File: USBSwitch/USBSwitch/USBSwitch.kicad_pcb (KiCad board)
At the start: 2 copper layers, 41 x 32 mm, 17 parts, among them J1 Conn_01x01_Female, J2 Conn_01x01_Female, J3 USB_A, J4 USB_B_Micro

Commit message: Update USBSwitch
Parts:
- removed REF**: Jitter Icon, Jitter_Logos:Symbol_Jitter-Icon_CopperAndSilkScreenTop
- removed REF**: KiCAD Logo, Symbol:Symbol_KiCAD-Logo_CopperAndSilkScreenTop
- added H3: MountingHole_Pad, MountingHole:MountingHole_2.2mm_M2_Pad_Via, F.Cu at (54.0, 32.0)
- added H4: MountingHole_Pad, MountingHole:MountingHole_2.2mm_M2_Pad_Via, F.Cu at (87.5, 66.0)
- moved H1 5.30 mm to (87.5, 32.0)
- moved H2 3.42 mm to (54.0, 66.0)
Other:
- board size 41 x 32 mm -> 41 x 40 mm

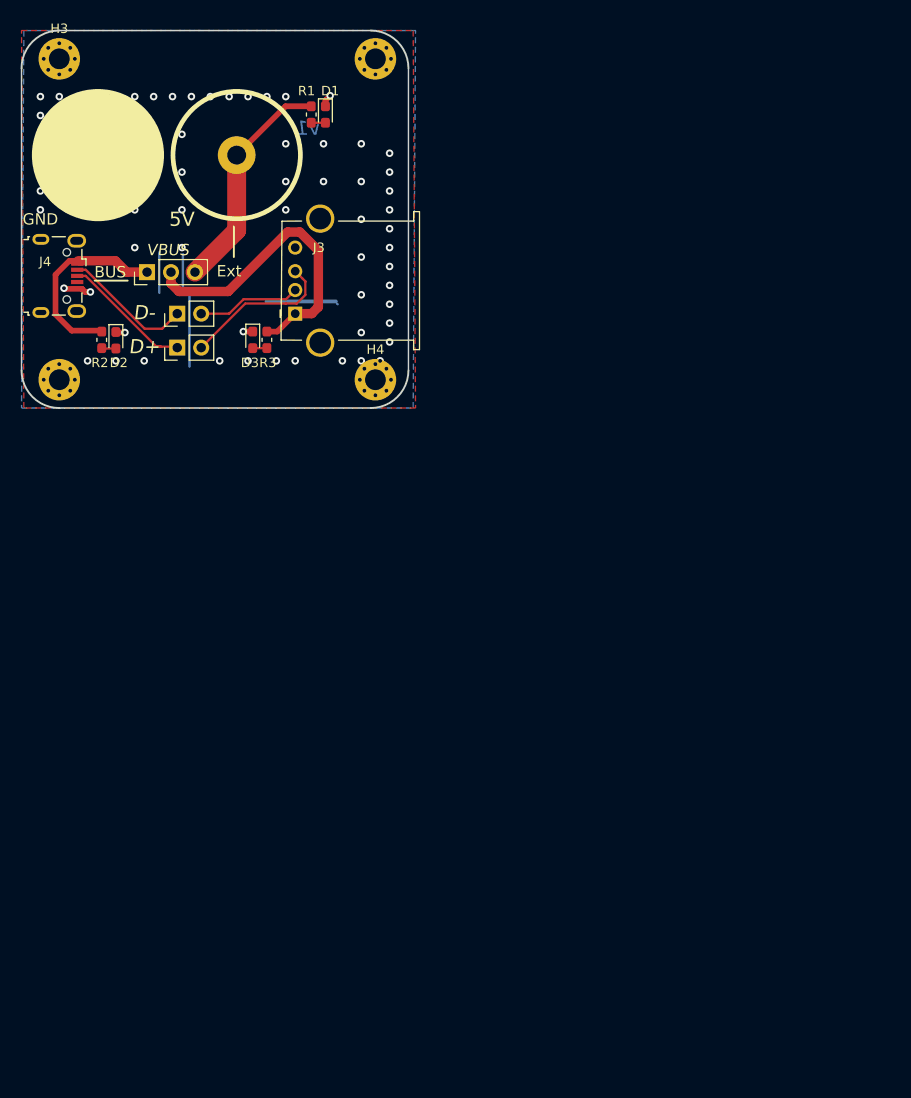
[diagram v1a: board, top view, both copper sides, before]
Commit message: USBSwitch ( =MITM board ): release V2
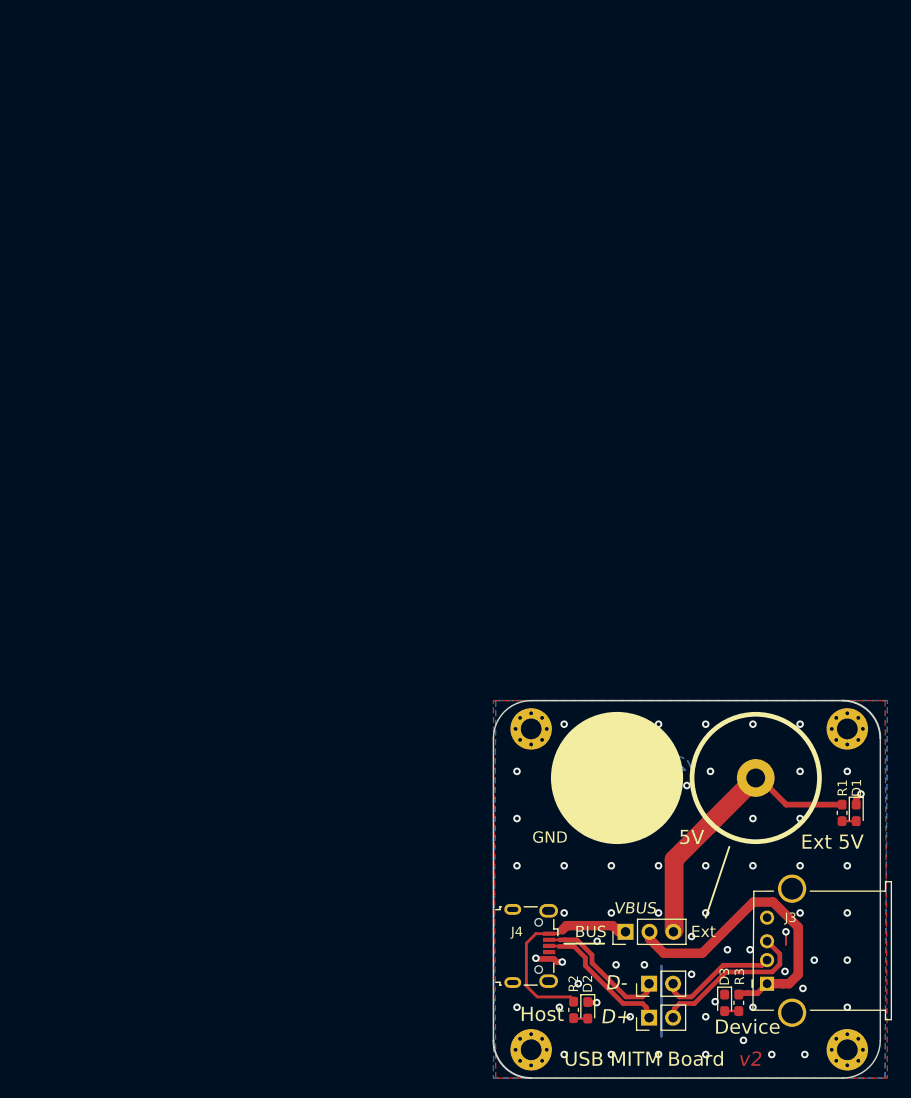
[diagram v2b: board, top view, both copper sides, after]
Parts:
- added REF**: Jitter Icon, Jitter_Logos:Symbol_Jitter-Icon_CopperAndSilkScreenTop, B.Cu at (115.0, 113.5)
- moved D1 93.0 mm to (138.4, 111.9)
- moved R1 93.0 mm to (136.9, 111.9)
- moved D2 86.8 mm to (110.0, 132.8)
- moved H1 86.8 mm to (137.5, 103.0)
- moved H2 86.8 mm to (104.0, 137.0)
- moved H3 86.8 mm to (104.0, 103.0)
- moved H4 86.8 mm to (137.5, 137.0)
- moved J3 86.8 mm to (129.0, 130.0)
- moved J4 86.8 mm to (104.0, 126.0)
- moved JP2 86.8 mm to (116.5, 133.6)
- moved JP3 86.8 mm to (116.5, 130.0)
- moved R2 86.8 mm to (108.5, 132.8)
- moved JP1 86.4 mm to (114.0, 124.5)
- moved D3 86.2 mm to (124.5, 132.0)
- moved R3 86.2 mm to (126.0, 132.0)
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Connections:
- net /D+ renamed /HOST_D+
- net /D- renamed /HOST_D-
- net Net-(J3-Pad2) renamed /DEVICE_D-
- net Net-(J3-Pad3) renamed /DEVICE_D+
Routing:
- net GND: track 29.1 -> 14.2 mm, vias 66 -> 61
- net +5V: track 24.3 -> 30.2 mm
- net /DEVICE_D-: track 11.0 -> 12.4 mm
- net /HOST_D-: track 13.9 -> 15.1 mm
- net VBUS: track 20.7 -> 21.8 mm
- net /DEVICE_D+: track 16.2 -> 17.2 mm
- net VCC: track 33.1 -> 32.6 mm
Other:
- net class USB added: clearance 0.2, trace_width 0.25, via_dia 0.8, via_drill 0.4
- board text added: "Device"
- board text added: "Ext 5V"
- board text added: "Host"
- board text added: "https://jitter.company"
- board text added: "v2"
- board text removed: "blinky101.github.io"
- board text removed: "v1"
